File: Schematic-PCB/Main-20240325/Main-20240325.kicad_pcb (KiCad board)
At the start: 2 copper layers, 102 x 102 mm, 77 parts, among them J1 Conn_01x10_Pin, J2 Conn_01x03_Pin, J3 Conn_01x15_Pin, J4 Conn_02x05_Odd_Even, J5 Conn_01x04_Pin, J6 Conn_01x05_Pin, U1 DEV-16771, U10 TSSP58038, U11 TSSP58038, U12 TSSP58038, U13 TSSP58038, U14 TSSP58038, U15 TSSP58038, U16 TSSP58038, U17 TSSP58038, U18 TSSP58038, U19 TSSP58038, U20 74AHC1G32, U4 TSSP58038, U5 TSSP58038, U6 TSSP58038, U7 TSSP58038, U8 TSSP58038, U9 TSSP58038

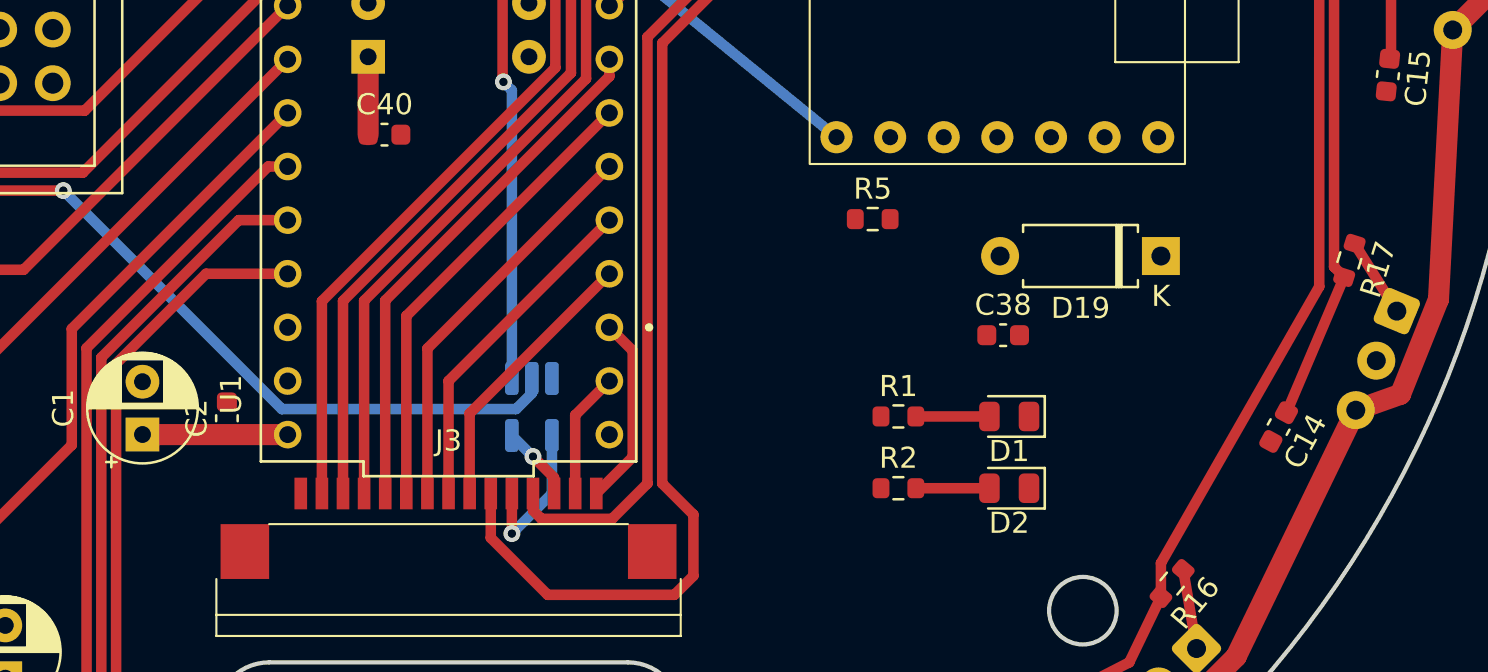
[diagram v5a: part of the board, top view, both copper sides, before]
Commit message: 配線を進めた
コネクタ以外ほぼ終わり
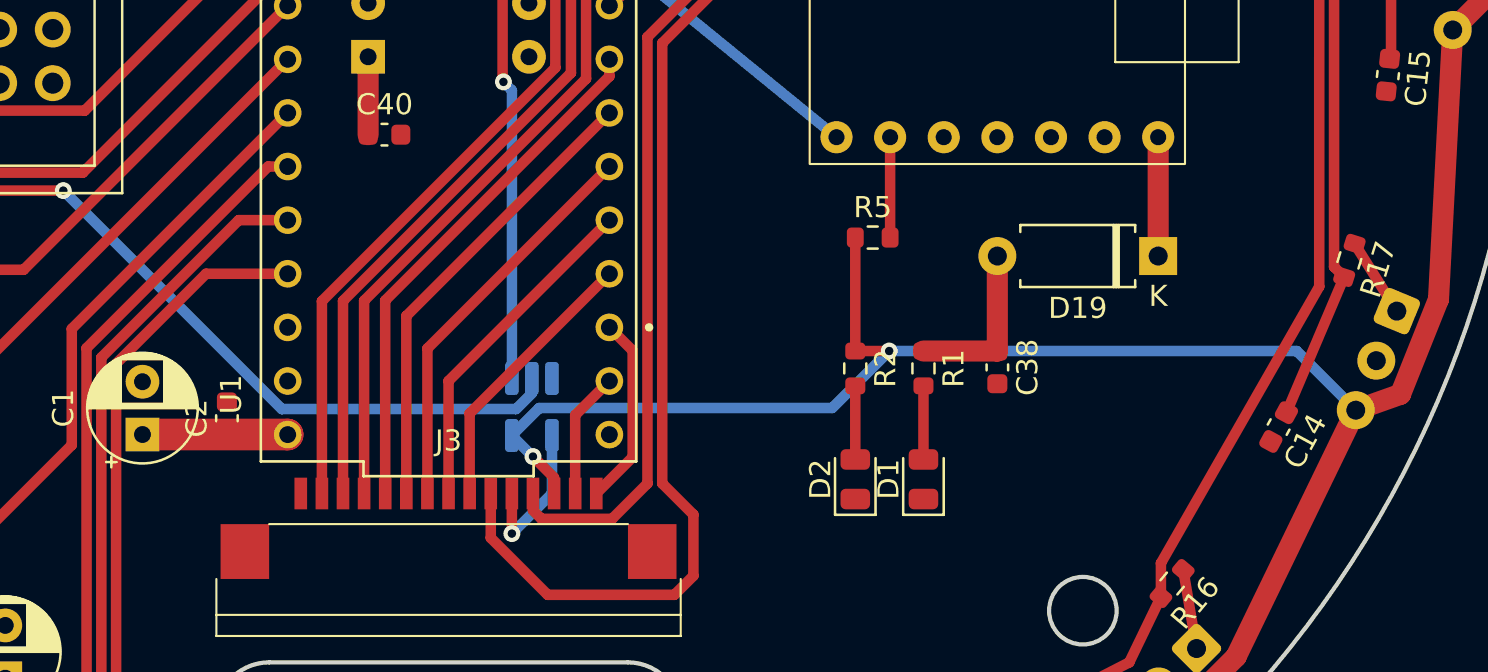
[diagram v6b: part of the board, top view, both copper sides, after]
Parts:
- moved D2 7.30 mm to (19.3, 23.8), turned to 90 degrees
- moved R2 6.03 mm to (19.3, 18.6), turned to -90 degrees
- moved D1 5.04 mm to (22.5, 23.8), turned to 90 degrees
- moved R1 2.57 mm to (22.5, 18.6), turned to -90 degrees
- moved C38 1.55 mm to (26.0, 18.5), turned to -90 degrees
- moved R5 0.88 mm to (20.1, 12.4)
- moved D19 0.13 mm to (33.6, 13.2)
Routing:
- net +3.3V: track 348.4 -> 398.2 mm, vias 2 -> 3
- net +5V: track 6.88 -> 14.9 mm
- net Net-(D19-K): track 0.00 -> 5.63 mm
- net Net-(U2-SCK_D8): track 0.00 -> 4.75 mm

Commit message: update: メイン基板の回路図/PCBを編集した
ESP32周り / ボールセンサ配置
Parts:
- removed D19: D_Small, Diode_THT:D_A-405_P7.62mm_Horizontal
- removed JP1, JP3, JP5, JP7: Jumper_2_Small_Bridged, Jumper:SolderJumper-2_P1.3mm_Bridged_Pad1.0x1.5mm
- removed JP6, JP8: Jumper_2_Small_Open, Jumper:SolderJumper-2_P1.3mm_Open_Pad1.0x1.5mm
- removed R5: 10K, Resistor_SMD:R_0603_1608Metric
- removed U2: ~, @2024TOINIOT2-Main:XIAO ESP32C3
- added D3: D_Small, Diode_THT:D_A-405_P7.62mm_Horizontal, F.Cu at (118.0, 60.5)
- added U21: ESP32-DEVKITC, @2024TOINIOT2-Line:ESP32-DEVKITC, F.Cu at (0.00, -6.27)
- J4: value Conn_02x05_Odd_Even -> Pixy 2.1
- U20: moved to F.Cu
- moved R3 163.5 mm to (131.0, 41.0), turned to 0 degrees
- moved R4 163.3 mm to (131.0, 43.5)
- moved C2 141.9 mm to (131.0, 31.0), turned to 0 degrees
- moved C39 136.6 mm to (111.8, 65.2), turned to 0 degrees
- moved C1 131.6 mm to (111.8, 58.6), turned to 0 degrees
- moved U20 123.7 mm to (119.3, 65.1), turned to 0 degrees
- moved D2 113.7 mm to (124.4, 67.2), turned to 0 degrees
- moved R2 113.5 mm to (131.0, 38.5), turned to 0 degrees
- moved R1 109.9 mm to (131.0, 36.0), turned to 0 degrees
- moved D1 109.6 mm to (124.4, 64.1), turned to 0 degrees
- moved C38 106.1 mm to (131.0, 33.5), turned to 0 degrees
- moved J5 63.7 mm to (98.8, 58.7)
- moved J6 48.5 mm to (124.4, 56.9)
- moved J2 46.7 mm to (98.8, 66.5)
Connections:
- J4 pad 1: Cam-MISO_RX -> MISO
- J4 pad 3: Net-(J4-Pin_3) -> SCK
- J4 pad 4: Cam-MOSI_TX -> MOSI
- J4 pad 7: Net-(J4-Pin_7) -> SS
- U1 pad 10: Cam_SS -> SS
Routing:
- net +3.3V: track 398.2 -> 3.69 mm, vias 3 -> 0
- net SDA: track 90.8 -> 0.00 mm
- net SCL: track 79.3 -> 0.00 mm
- net ball11: track 83.6 -> 7.37 mm
- net SW-TAC-3: track 74.1 -> 0.00 mm
- net ball01k: track 67.0 -> 0.00 mm
- net SW-TAC-4: track 62.3 -> 0.00 mm
- net ball13: track 69.0 -> 7.01 mm, vias 1 -> 0
- net ball12: track 68.3 -> 6.99 mm
- net ball10: track 65.2 -> 6.99 mm
- net KickerSignal-Main: track 58.0 -> 0.00 mm, vias 1 -> 0
- net ball03: track 63.1 -> 7.37 mm, vias 1 -> 0
- net Cam_SS: track 55.6 -> 0.00 mm, vias 1 -> 0
- net ball02k: track 54.2 -> 0.00 mm
- net KickerSignal-UI: track 52.8 -> 0.00 mm, vias 1 -> 0
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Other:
- copper layers 2 -> 4

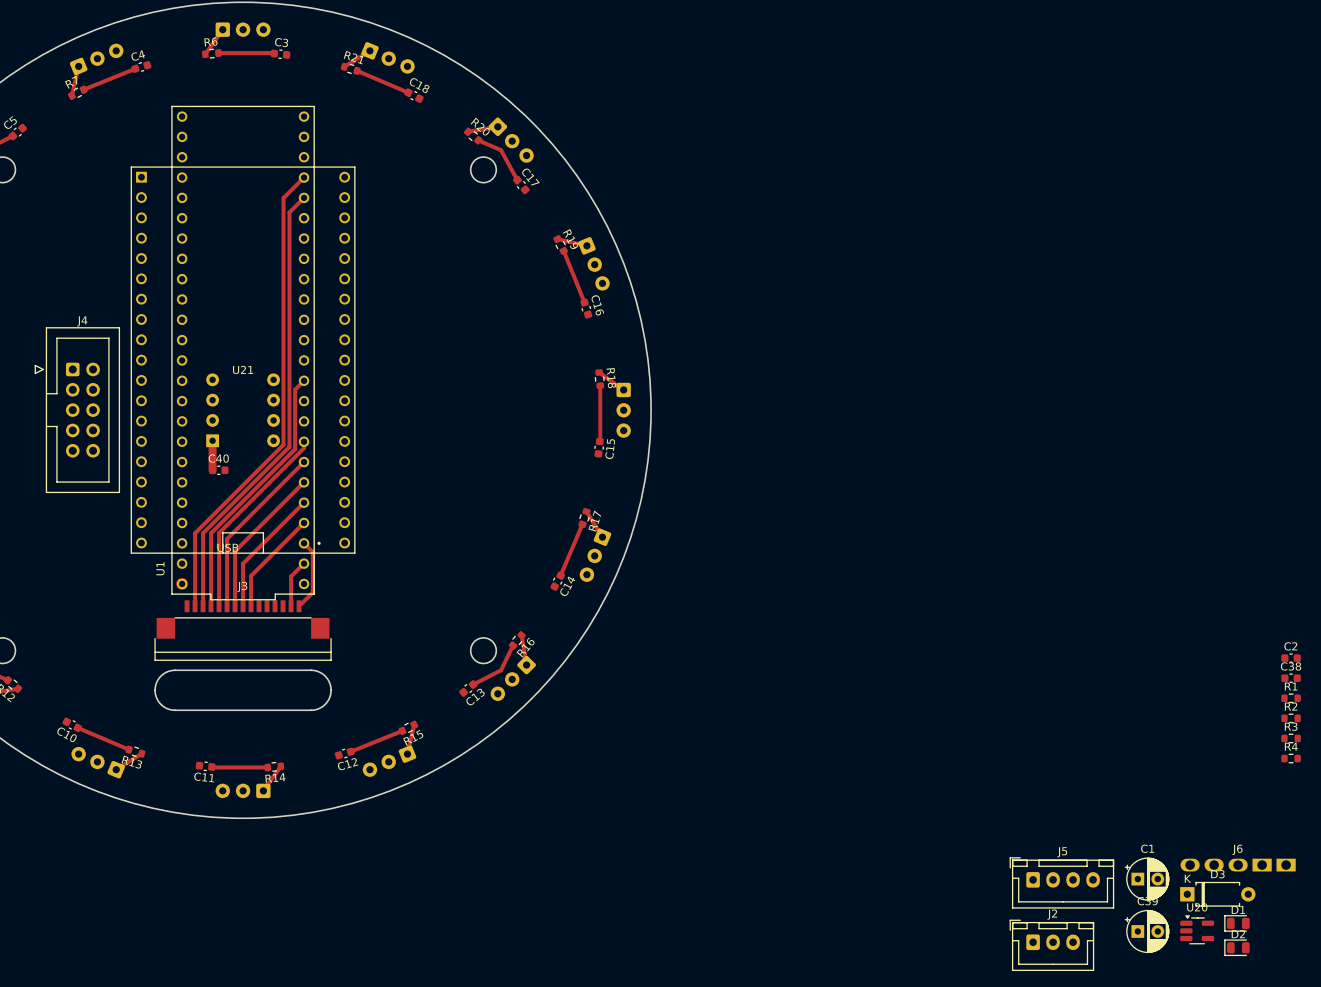
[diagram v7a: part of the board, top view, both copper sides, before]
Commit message: update: メイン基板のピン割り当てをUIに合わせた
タクトスイッチ、キッカー信号
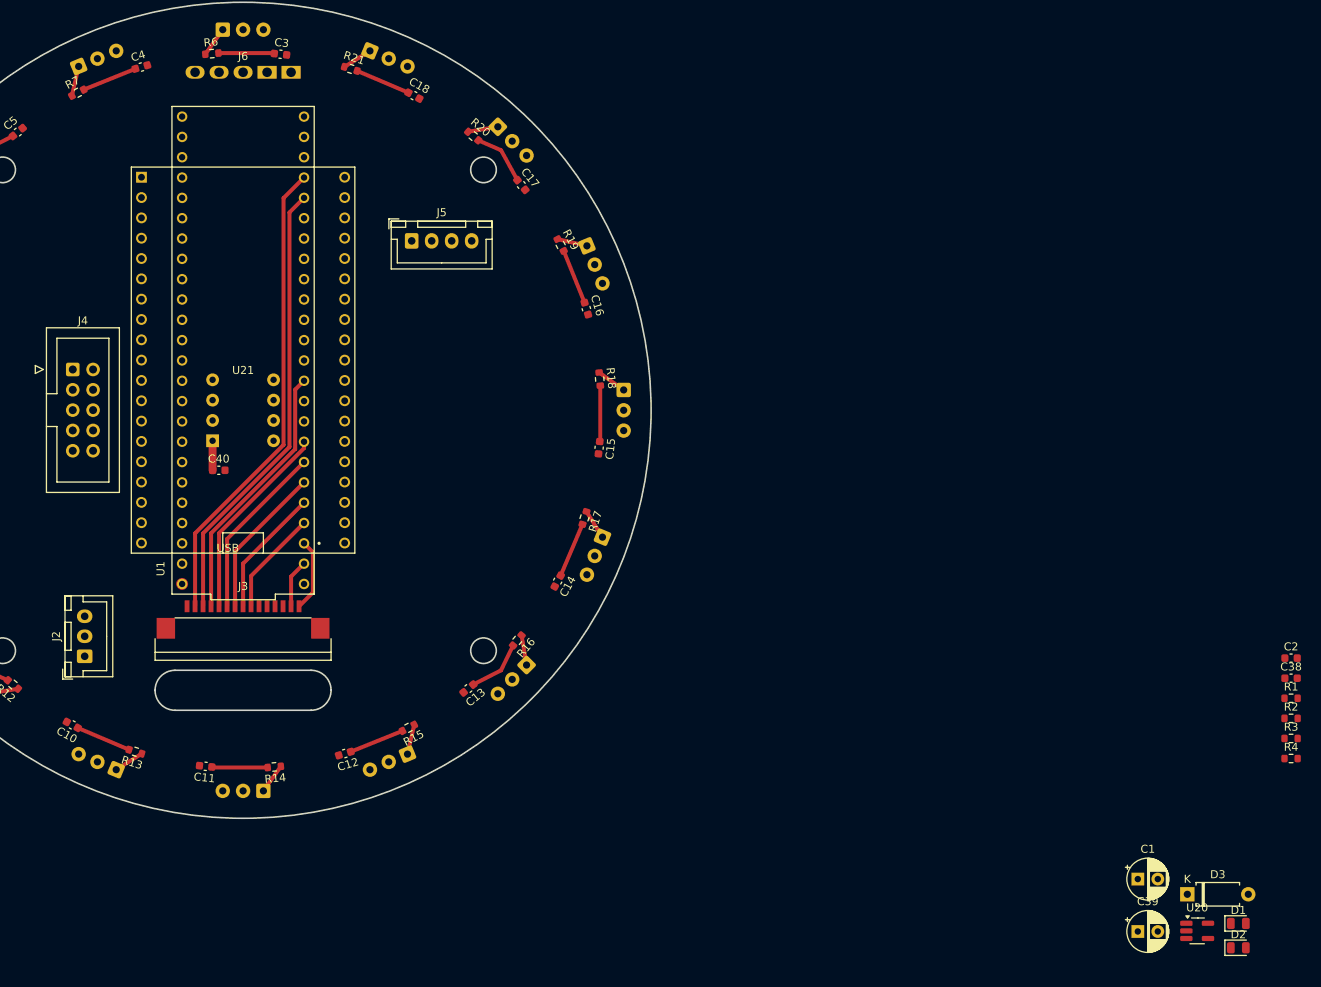
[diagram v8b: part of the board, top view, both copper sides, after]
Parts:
- moved J6 159.0 mm to (0.00, -42.2)
- moved J2 123.8 mm to (-19.8, 30.8), turned to 90 degrees
- moved J5 111.4 mm to (21.1, -21.2)
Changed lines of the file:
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@@
 	(footprint "Connector_JST:JST_XH_B3B-XH-A_1x03_P2.50mm_Vertical"
 		(layer "F.Cu")
-		(at 98.75 66.5)
+		(at -19.8 30.75 90)
 		(descr "JST XH series connector, B3B-XH-A (http://www.jst-mfg.com/product/pdf/eng/eXH.pdf), generated with kicad-footprint-generator")
 		(tags "connector JST XH vertical")
 		(property "Reference" "J2"
-			(at 2.5 -3.55 0)
+			(at 2.5 -3.55 270)
 			(layer "F.SilkS")
 			(effects
@@
 		)
 		(property "Value" "Conn_01x03_Pin"
-			(at 2.5 4.6 0)
+			(at 2.5 4.6 270)
 			(layer "F.Fab")
 			(effects
@@
 		)
 		(property "Footprint" "Connector_JST:JST_XH_B3B-XH-A_1x03_P2.50mm_Vertical"
-			(at 0 0 0)
+			(at 0 0 90)
 			(unlocked yes)
 			(layer "F.Fab")
@@
 		)
 		(property "Datasheet" ""
-			(at 0 0 0)
+			(at 0 0 90)
 			(unlocked yes)
 			(layer "F.Fab")
@@
 		)
 		(property "Description" "Generic connector, single row, 01x03, script generated"
-			(at 0 0 0)
+			(at 0 0 90)
 			(unlocked yes)
 			(layer "F.Fab")
@@
 		(attr through_hole)
 		(fp_line
-			(start -2.85 -2.75)
-			(end -2.85 -1.5)
+			(start -1.6 -2.75)
+			(end -2.85 -2.75)
 			(stroke
 				(width 0.12)
@@
 		)
 		(fp_line
-			(start -2.56 -2.46)
-			(end -2.56 3.51)
+			(start -2.85 -2.75)
+			(end -2.85 -1.5)
 			(stroke
 				(width 0.12)
@@
 		)
 		(fp_line
-			(start -2.56 3.51)
-			(end 7.56 3.51)
+			(start 7.56 -2.46)
+			(end -2.56 -2.46)
 			(stroke
 				(width 0.12)
@@
 		)
 		(fp_line
-			(start -2.55 -2.45)
-			(end -2.55 -1.7)
+			(start -2.56 -2.46)
+			(end -2.56 3.51)
 			(stroke
 				(width 0.12)
@@
 		)
 		(fp_line
-			(start -2.55 -1.7)
-			(end -0.75 -1.7)
+			(start 7.55 -2.45)
+			(end 5.75 -2.45)
 			(stroke
 				(width 0.12)
@@
 		)
 		(fp_line
-			(start -2.55 -0.2)
-			(end -1.8 -0.2)
+			(start 5.75 -2.45)
+			(end 5.75 -1.7)
 			(stroke
 				(width 0.12)
@@
 		)
 		(fp_line
-			(start -1.8 -0.2)
-			(end -1.8 2.75)
+			(start 4.25 -2.45)
+			(end 0.75 -2.45)
 			(stroke
 				(width 0.12)
@@
 		)
 		(fp_line
-			(start -1.8 2.75)
-			(end 2.5 2.75)
+			(start 0.75 -2.45)
+			(end 0.75 -1.7)
 			(stroke
 				(width 0.12)
@@
 		)
 		(fp_line
-			(start -1.6 -2.75)
-			(end -2.85 -2.75)
+			(start -0.75 -2.45)
+			(end -2.55 -2.45)
 			(stroke
 				(width 0.12)
@@
 		)
 		(fp_line
-			(start -0.75 -2.45)
-			(end -2.55 -2.45)
+			(start -2.55 -2.45)
+			(end -2.55 -1.7)
 			(stroke
 				(width 0.12)
@@
 		)
 		(fp_line
-			(start -0.75 -1.7)
-			(end -0.75 -2.45)
+			(start 7.55 -1.7)
+			(end 7.55 -2.45)
 			(stroke
 				(width 0.12)
@@
 		)
 		(fp_line
-			(start 0.75 -2.45)
-			(end 0.75 -1.7)
+			(start 5.75 -1.7)
+			(end 7.55 -1.7)
 			(stroke
 				(width 0.12)
@@
 		)
 		(fp_line
-			(start 0.75 -1.7)
-			(end 4.25 -1.7)
+			(start 4.25 -1.7)
+			(end 4.25 -2.45)
 			(stroke
 				(width 0.12)
@@
 		)
 		(fp_line
-			(start 4.25 -2.45)
-			(end 0.75 -2.45)
+			(start 0.75 -1.7)
+			(end 4.25 -1.7)
 			(stroke
 				(width 0.12)
@@
 		)
 		(fp_line
-			(start 4.25 -1.7)
-			(end 4.25 -2.45)
+			(start -0.75 -1.7)
+			(end -0.75 -2.45)
 			(stroke
 				(width 0.12)
@@
 		)
 		(fp_line
-			(start 5.75 -2.45)
-			(end 5.75 -1.7)
+			(start -2.55 -1.7)
+			(end -0.75 -1.7)
 			(stroke
 				(width 0.12)
@@
 		)
 		(fp_line
-			(start 5.75 -1.7)
-			(end 7.55 -1.7)
+			(start 7.55 -0.2)
+			(end 6.8 -0.2)
 			(stroke
 				(width 0.12)
@@
 		)
 		(fp_line
-			(start 6.8 2.75)
-			(end 2.5 2.75)
+			(start -1.8 -0.2)
+			(end -1.8 2.75)
 			(stroke
 				(width 0.12)
@@
 		)
 		(fp_line
-			(start 7.55 -2.45)
-			(end 5.75 -2.45)
+			(start -2.55 -0.2)
+			(end -1.8 -0.2)
 			(stroke
 				(width 0.12)
@@
 		)
 		(fp_line
-			(start 7.55 -1.7)
-			(end 7.55 -2.45)
+			(start 6.8 2.75)
+			(end 2.5 2.75)
 			(stroke
 				(width 0.12)
@@
 		)
 		(fp_line
-			(start 7.55 -0.2)
-			(end 6.8 -0.2)
+			(start -1.8 2.75)
+			(end 2.5 2.75)
 			(stroke
 				(width 0.12)
@@
 		)
 		(fp_line
-			(start 7.56 -2.46)
-			(end -2.56 -2.46)
+			(start 7.56 3.51)
+			(end 7.56 -2.46)
 			(stroke
 				(width 0.12)
@@
 		)
 		(fp_line
-			(start 7.56 3.51)
-			(end 7.56 -2.46)
+			(start -2.56 3.51)
+			(end 7.56 3.51)
 			(stroke
 				(width 0.12)
@@
 		)
 		(fp_line
-			(start -2.95 -2.85)
-			(end -2.95 3.9)
+			(start 7.95 -2.85)
+			(end -2.95 -2.85)
 			(stroke
 				(width 0.05)
@@
 		)
 		(fp_line
-			(start -2.95 3.9)
-			(end 7.95 3.9)
+			(start -2.95 -2.85)
+			(end -2.95 3.9)
 			(stroke
 				(width 0.05)
@@
 		)
 		(fp_line
-			(start 7.95 -2.85)
-			(end -2.95 -2.85)
+			(start 7.95 3.9)
+			(end 7.95 -2.85)
 			(stroke
 				(width 0.05)
@@
 		)
 		(fp_line
-			(start 7.95 3.9)
-			(end 7.95 -2.85)
+			(start -2.95 3.9)
+			(end 7.95 3.9)
 			(stroke
 				(width 0.05)
@@
 		)
 		(fp_line
-			(start -2.45 -2.35)
-			(end -2.45 3.4)
+			(start 7.45 -2.35)
+			(end -2.45 -2.35)
 			(stroke
 				(width 0.1)
@@
 		)
 		(fp_line
-			(start -2.45 3.4)
-			(end 7.45 3.4)
+			(start -0.625 -2.35)
+			(end 0 -1.35)
 			(stroke
 				(width 0.1)
@@
 		)
 		(fp_line
-			(start -0.625 -2.35)
-			(end 0 -1.35)
+			(start -2.45 -2.35)
+			(end -2.45 3.4)
 			(stroke
 				(width 0.1)
@@
 		)
 		(fp_line
-			(start 7.45 -2.35)
-			(end -2.45 -2.35)
+			(start 7.45 3.4)
+			(end 7.45 -2.35)
 			(stroke
 				(width 0.1)
@@
 		)
 		(fp_line
-			(start 7.45 3.4)
-			(end 7.45 -2.35)
+			(start -2.45 3.4)
+			(end 7.45 3.4)
 			(stroke
 				(width 0.1)
@@
 		)
 		(fp_text user "${REFERENCE}"
-			(at 2.5 2.7 0)
+			(at 2.5 2.7 270)
 			(layer "F.Fab")
 			(effects
@@
 		)
 		(pad "1" thru_hole roundrect
-			(at 0 0)
+			(at 0 0 90)
 			(size 1.7 1.95)
 			(drill 0.95)
@@
 		)
 		(pad "2" thru_hole oval
-			(at 2.5 0)
+			(at 2.5 0 90)
 			(size 1.7 1.95)
 			(drill 0.95)
@@
 		)
 		(pad "3" thru_hole oval
-			(at 5 0)
+			(at 5 0 90)
 			(size 1.7 1.95)
 			(drill 0.95)
@@
 	(footprint "@2024TOINIOT2-Main:Connector"
 		(layer "F.Cu")
-		(at 124.38 56.85)
+		(at 0 -42.25)
 		(property "Reference" "J6"
 			(at 0 -2 0)
@@
 	(footprint "Connector_JST:JST_XH_B4B-XH-A_1x04_P2.50mm_Vertical"
 		(layer "F.Cu")
-		(at 98.75 58.7)
+		(at 21.075 -21.175)
 		(descr "JST XH series connector, B4B-XH-A (http://www.jst-mfg.com/product/pdf/eng/eXH.pdf), generated with kicad-footprint-generator")
 		(tags "connector JST XH vertical")
